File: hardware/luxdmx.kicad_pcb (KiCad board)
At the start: 4 copper layers, 119 x 79 mm, 101 parts, among them J1 XLR-5 NC5FAH, J2 USB-C, J3 HY931147C, J4 DISP SH9, J5 XLR-5 NC5FAH, J6 EXP SH9, J7 DMX-OUT A, J8 DMX-OUT B, Q1 MMBT3904, Q2 MMBT3904, SW1 BOOT, SW2 RST, U1 ESP32-S3-WROOM-1-N8, U2 W5500, U3 CH340C, U4 SY8089, U5 ISO3086DWR, U6 ISO3086DWR, U7 DP9900M-5V, U8 USBLC6-2SC6, U9 TPS2116DRLR, Y1 25MHz

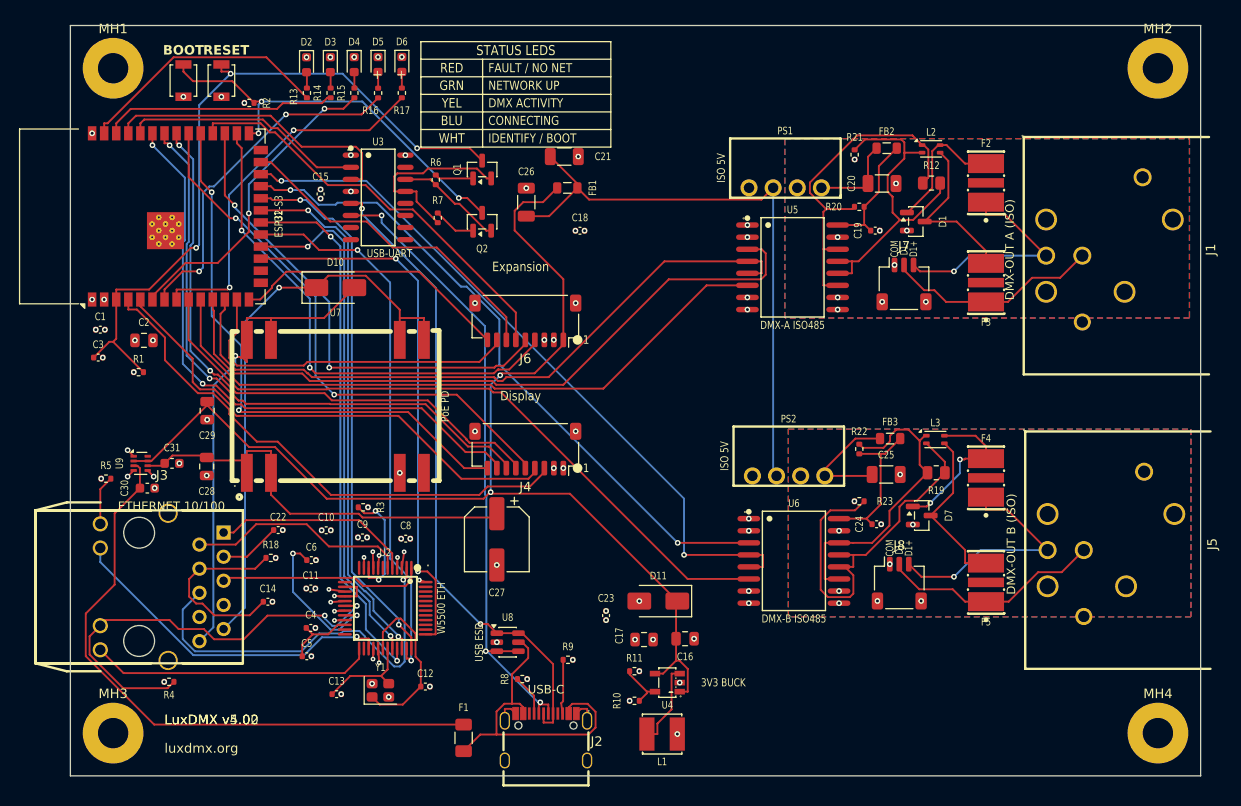
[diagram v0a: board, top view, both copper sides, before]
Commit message: hw: v5 re-route on a new placement + reproducible routing/validation pipeline
Re-routed the whole board from scratch on the current placement and gave it a
proper hands-off pipeline. Two commands now: route_all.sh (setup_netclasses,
rebuild_iso, escape, Freerouting loop, finish_partial, maze, cleanup, tighten,
widen_eth) and validate_all.sh (7-gate production verdict + exit code).

Net classes replace the old global-thin-then-widen approach: Default 0.20 /
Power 0.40 / Fine 0.15mm (Fine is only the W5500-dense nets), and Freerouting
routes each net at its class width in one pass.

validate_all.sh gates on connectivity, DRC, geometry/DFM + current, DMX isolation,
electrical, EMC placement and the new validate_critical (eth/SPI/crystal length,
vias, intra-pair skew, detour, net-class widths). All 7 hard gates pass.

widen_eth widens the MDI pairs toward ~50 ohm single-ended (RXN/RXP/TXP to ~0.34mm,
ETH_TXN stays 0.15mm in a dense corridor). Still single-ended and not length-matched;
coupled diff-pair routing stays a supervised GUI job.

DRC rules aligned to the relaxed but JLC-safe spec (min track 0.15, hole-to-hole
0.2, vias 0.5/0.2 = 0.15mm annular, min-annular 0.13). Escape-via drill 0.25 -> 0.20
so the annular is 0.15mm not 0.125. The DMX iso B-pour check now gates only the
fault-exposed cable-side nets; a REST net behind the TBU may take a short B.Cu hop
(the cut is bridged by the F.Cu pour + stitch vias, keepouts make Freerouting choke).

Fab package regenerated, all hard-gated on 0 unrouted. Still a first-spin prototype:
never fabricated, and the eth is not controlled-impedance / not coupled.
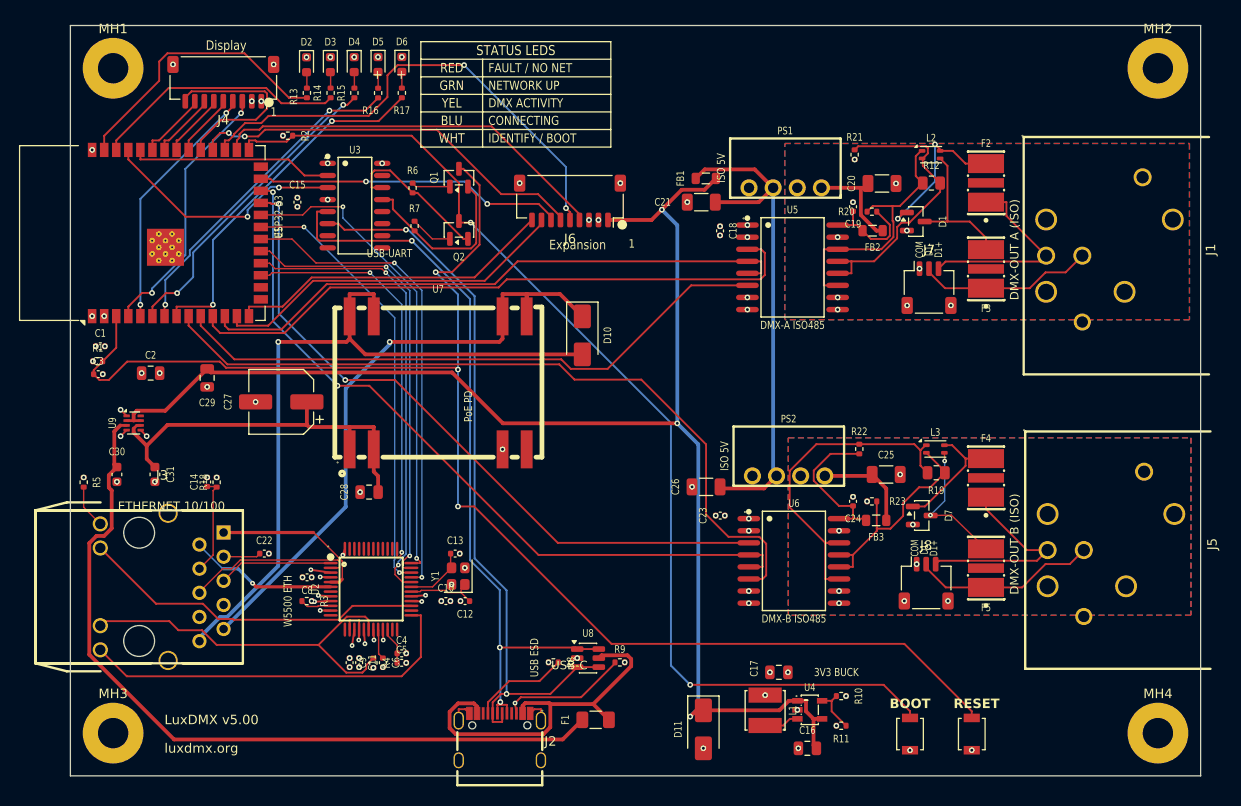
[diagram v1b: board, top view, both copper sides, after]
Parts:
- moved SW2 104.8 mm to (192.5, 163.5)
- moved SW1 102.9 mm to (186.0, 163.5)
- moved J4 50.0 mm to (113.7, 94.9)
- moved C26 35.4 mm to (164.5, 137.5), turned to 180 degrees
- moved C27 26.9 mm to (119.8, 128.5), turned to 180 degrees
- moved D10 26.5 mm to (151.5, 121.5), turned to -90 degrees
- moved R11 22.5 mm to (178.8, 162.6), turned to 180 degrees
- moved R10 21.8 mm to (178.8, 159.5), turned to 180 degrees
- moved R4 21.6 mm to (129.5, 156.0), turned to 90 degrees
- moved C13 19.4 mm to (138.1, 144.5)
- moved C28 17.3 mm to (129.1, 138.0), turned to 180 degrees
- moved C16 17.3 mm to (175.2, 165.0), turned to 180 degrees
- moved C23 16.0 mm to (166.0, 140.5), turned to 180 degrees
- moved U4 15.3 mm to (175.4, 160.9), turned to 180 degrees
- moved C21 15.2 mm to (164.0, 107.5), turned to 180 degrees
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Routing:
- net EN: track 75.1 -> 151.2 mm
- net IO0: track 43.0 -> 114.0 mm, vias 3 -> 2
- net DISP_MOSI: track 63.5 -> 6.85 mm, vias 2 -> 0
- net DISP_CS: track 63.6 -> 7.13 mm, vias 2 -> 0
- net DISP_DC: track 63.6 -> 7.38 mm, vias 2 -> 0
- net DISP_SCK: track 58.0 -> 6.64 mm, vias 2 -> 0
- net DISP_RST: track 59.7 -> 20.3 mm, vias 2 -> 0
- net DISP_SDA: track 56.0 -> 28.2 mm, vias 0 -> 2
- net +5V: track 125.5 -> 151.5 mm, vias 2 -> 3
- net DISP_SCL: track 52.2 -> 26.7 mm, vias 0 -> 2
- net VPOE-: track 52.6 -> 77.8 mm
- net ETH_TXP: track 42.4 -> 17.9 mm, vias 1 -> 0
- net DMX2_B: track 42.1 -> 24.1 mm
- net +5V_USBF: track 65.7 -> 83.6 mm
- net ETH_RST: track 57.1 -> 44.2 mm
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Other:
- board text removed: "LuxDMX v4.02"

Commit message: hw: BOM sourcing sweep, move every out-of-stock part to an in-stock JLC part (#66)
The board kept having parts go "not available at JLC" in waves. Root cause found: JLC
decides on minPurchaseNum, not raw stock. A part can show 400k stock but a 4-figure
min-buy, which means the free-assembly reel is exhausted, so it is effectively out of
stock. And the E96 values (45.3k, 150R, 330R, 470R) have no JLC Basic part at all (the
Basic 0402 resistor library is E24 only), so those move to the Fenghua FRC0402 line
(min-buy 1, real stock).

Swaps (all same footprint/value, no re-route):
  R10 45.3k 1%   C137977 (16 pcs)  to C2933099
  R14/16/17 150R C25082 (OOS)      to C2909321
  R4/5 330R      C25104            to C2930002
  R20-23 470R    C25117            to C2909361
  R13/15 1k      C11702            to C106235
  FB1-3 600R     C139168           to C1017 (JLC Basic)
  Y1 25MHz xtal  C2981622 (CL20pF) to C2981624 (in-stock 2520, CL 9pF)
  C12/C13 load   33pF (stale 22pF) to 10pF C0G C32949 (matches the 9pF crystal)

U3 CH340C (C84681) was flagged "no longer manufactured" at JLC, swapped to C7464026,
the same CH340C in the same SOP-16 with an active SKU. That one would have blocked the
whole order.

The durable crystal fix is a mainstream 3225 package (C9006, JLC Basic ~247k), but that
footprint swap needs a supervised re-route of the packed W5500 corner, so it is left for
a later spin (noted in luxdmx.py). validate_all 7/7 hard gates pass, fab package
(BOM/CPL/gerbers) regenerated. This is the revision sent to fab.

Co-authored-by: Thomas <tombueng@gmail.com>
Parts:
- C12, C13: value 33pF C0G -> 10pF C0G
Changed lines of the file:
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@@
 			)
 		)
-		(property "Value" "33pF C0G"
+		(property "Value" "10pF C0G"
 			(at 0 1.16 0)
 			(layer "F.Fab")
@@
 			)
 		)
-		(property "Value" "33pF C0G"
+		(property "Value" "10pF C0G"
 			(at 2 4.66 0)
 			(layer "F.Fab")

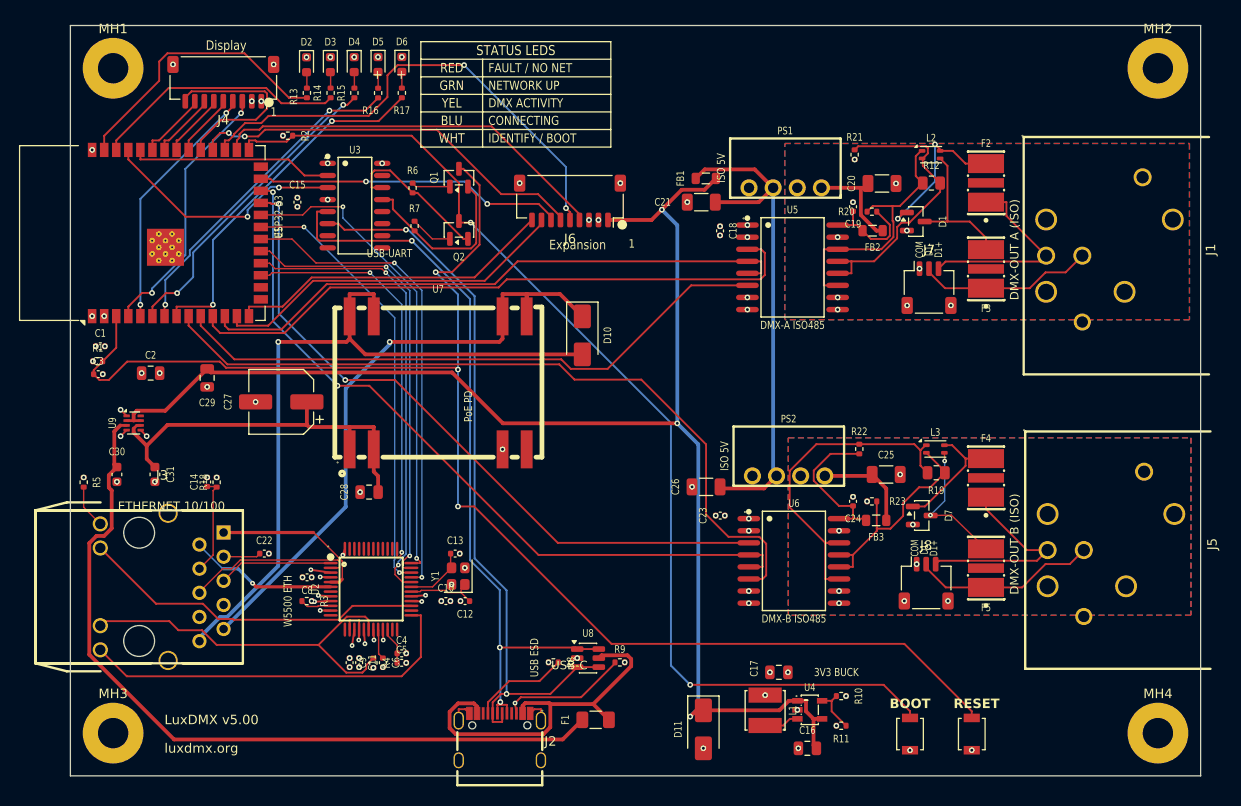
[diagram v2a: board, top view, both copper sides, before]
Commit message: hw: v5.2 -- native USB, TPS2116 priority mode, 3225 crystal (#80)
* hw: v5.2 -- native USB, TPS2116 priority mode, 3225 crystal

Fixes the two hardware defects the v5.00 first article turned up, and drops the
serial bridge while we're in there. Revision goes to v5.2.

The auto-reset transistors had EN and IO0 on the wrong collectors, so flashing
needed the manual BOOT-button dance and a tool asserting DTR or RTS alone could
yank either line. Rather than swap the collectors, the whole bridge is gone:
U3, Q1, Q2, R6, R7 and C15 removed. USB-C now goes straight to the S3's native
USB-Serial-JTAG on IO19/IO20, which is in ROM and gives us the flashing port,
the console and JTAG for free. esptool resets over USB by itself, so there is
no auto-reset circuit left to mis-wire. Six parts fewer, two fewer part numbers
to source, and UART0 is free now (broken out on J6 pins 8/9).

The PoE to USB handover hung the board. The suspected cause (too little cap on
the USB input) was wrong: MODE and PR1 were tied to GND, which selects the
TPS2116's default "higher voltage wins" mode, and two near-equal 5V sources
make that hunt. It runs in priority mode now, MODE on VIN1 so PoE always wins,
with a 30k/10k PR1 divider putting the switchover at 4.0V. Vsw is high on
purpose: VOUT tracks VIN1 down until the switch actually fires, so 4.0V keeps
the rail well clear of the ~2.8V where the ESP hangs.

Crystal moved from the 2520 to the 3225 package (C9006, CL 12pF, so 18pF C0G
load caps). The 2520 kept going out of stock at JLC, the 3225 is the mainstream
size that is always there. R24 also went to a 714k-stock SKU.

Board is fully routed: 0 unrouted, 0 hard DRC. The schematic was stale (it
still had the CH340), so it is regenerated from the netlist and round-trip
verified against it, 0 diff on real nets. BOM/CPL/gerbers regenerated, all 93
parts sourced against live JLC assembly stock (not LCSC retail, which is a
different pool and had me chasing a phantom shortage).

None of this is valida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
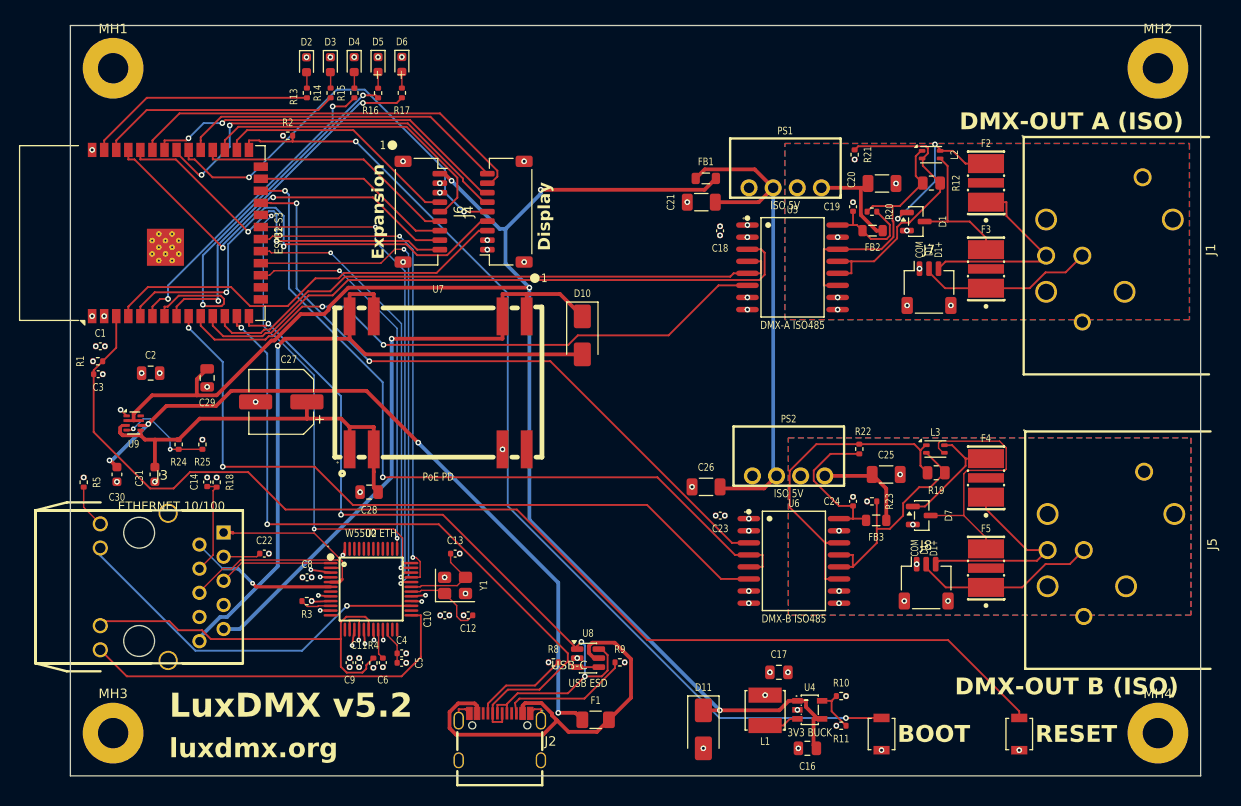
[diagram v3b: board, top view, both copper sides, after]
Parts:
- removed C15: 100nF, C_0402_1005Metric
- removed Q1, Q2: MMBT3904, SOT-23
- removed R6, R7: 10k, R_0402_1005Metric
- removed U3: CH340C, SOP-16_L10.0-W3.9-P1.27-LS6.0-BL
- added R24: 30k, R_0402_1005Metric, F.Cu at (109.0, 133.0)
- added R25: 10k, R_0402_1005Metric, F.Cu at (111.5, 133.0)
- C12, C13: value 10pF C0G -> 18pF C0G
- U1: value ESP32-S3-WROOM-1-N8 -> ESP32-S3-WROOM-1-N8R2
- Y1: footprint Crystal_SMD_2520-4Pin_2.5x2.0mm -> Crystal_SMD_3225-4Pin_3.2x2.5mm
- moved J4 32.8 mm to (143.5, 108.5), turned to 90 degrees
- moved J6 15.7 mm to (134.5, 108.5), turned to -90 degrees
- moved SW2 5.00 mm to (197.5, 163.5)
- moved SW1 3.00 mm to (183.0, 163.5)
- moved C12 1.54 mm to (139.5, 151.0)
- moved C10 1.50 mm to (137.0, 151.0)
- moved Y1 1.03 mm to (138.1, 147.8), turned to 0 degrees
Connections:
- J6 pad 8: EXP_IO19 -> S3_TX
- J6 pad 9: EXP_IO20 -> S3_RX
- U1 pad 13: EXP_IO19 -> USB_DM
- U1 pad 14: EXP_IO20 -> USB_DP
- U9 pad 3: +5V_USBF -> +5V_POE
- U9 pad 4: GND -> N$4
- U9 pad 5: GND -> +5V_POE
- U9 pad 6: +5V_POE -> +5V_USBF
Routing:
- net EXP_IO19: track 37.9 -> 0.00 mm
- net DISP_SCK: track 6.64 -> 43.8 mm, vias 0 -> 2
- net DISP_DC: track 7.38 -> 43.0 mm
- net EXP_IO20: track 34.6 -> 0.00 mm
- net DISP_MOSI: track 6.85 -> 41.1 mm, vias 0 -> 2
- net DISP_CS: track 7.13 -> 39.0 mm, vias 0 -> 2
- net EN: track 151.2 -> 124.9 mm, vias 3 -> 0
- net DISP_SCL: track 26.7 -> 50.3 mm
- net DTR: track 19.2 -> 0.00 mm
- net EXP_IO36: track 51.8 -> 32.8 mm, vias 2 -> 0
- net S3_RX: track 21.4 -> 40.0 mm, vias 0 -> 2
- net EXP_IO35: track 42.3 -> 26.0 mm
- net RTS: track 15.9 -> 0.00 mm
- net S3_TX: track 26.2 -> 41.9 mm
- net DISP_SDA: track 28.2 -> 43.8 mm, vias 2 -> 0
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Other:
- board text added: "LuxDMX v5.2"
- board text added: "LuxDMX v5.2 -- KEY FEATURES"
- board text removed: "BLU"
- board text removed: "CONNECTING"
- board text removed: "DMX ACTIVITY"
- board text removed: "FAULT / NO NET"
- board text removed: "GRN"
- board text removed: "IDENTIFY / BOOT"
- board text removed: "LuxDMX v5.00"
- board text removed: "LuxDMX v5.00 -- KEY FEATURES"
- board text removed: "NETWORK UP"
- board text removed: "RED"
- board text removed: "STATUS LEDS"
- board text removed: "USB-UART"
- board text removed: "WHT"
- board text removed: "YEL"
